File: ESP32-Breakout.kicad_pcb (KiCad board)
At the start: 2 copper layers, 44.5 x 49.5 mm, 3 parts, among them J101 Conn_01x19, J102 Conn_01x19, U101 ESP32-DEVKITC-32D

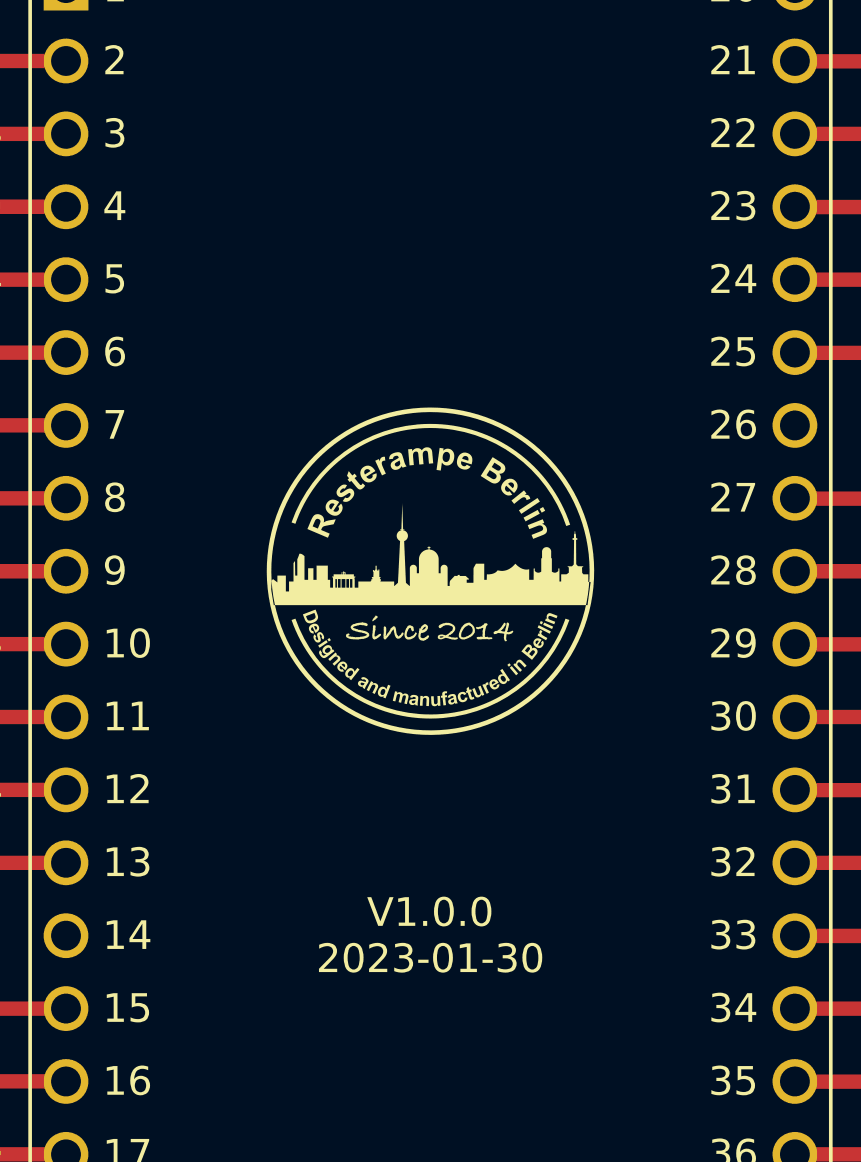
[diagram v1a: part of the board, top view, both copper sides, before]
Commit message: Documentation update, name of board on PCB
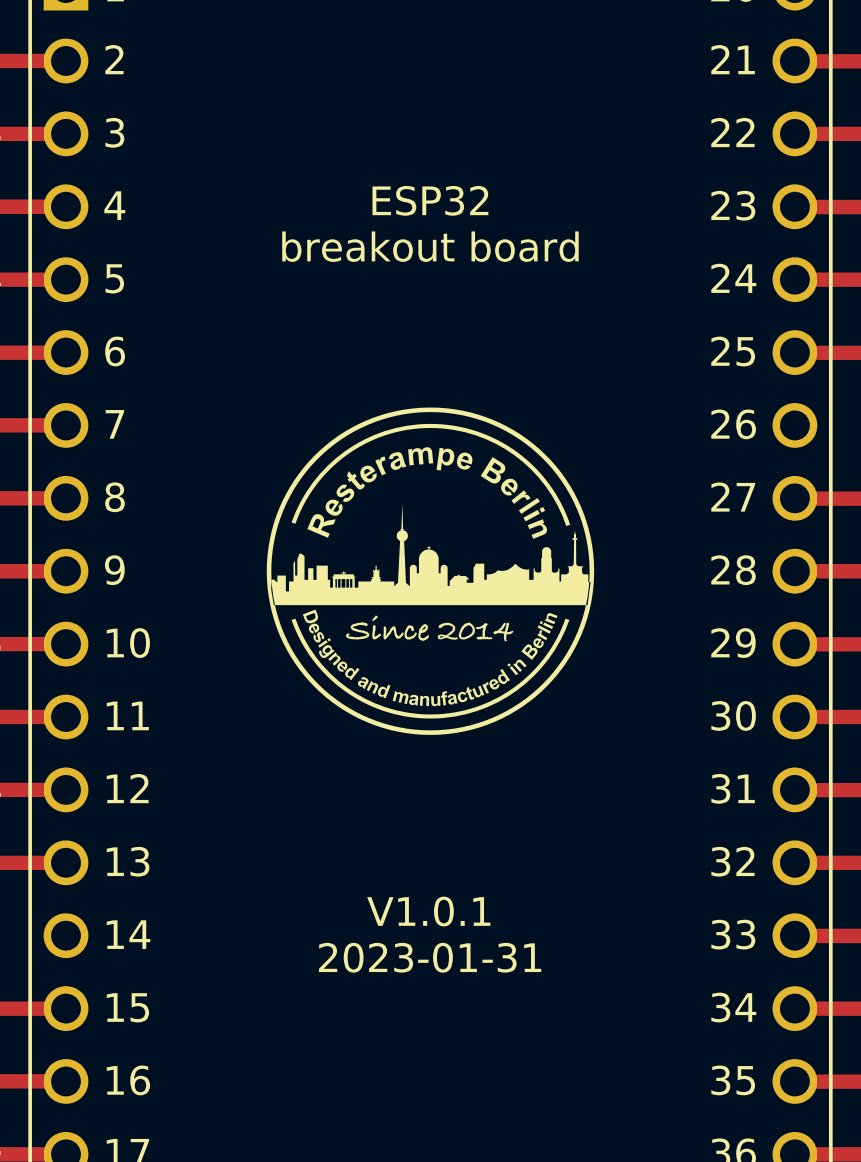
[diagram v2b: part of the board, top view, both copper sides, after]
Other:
- board text added: "ESP32 breakout board"
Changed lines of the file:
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@@
   (title_block
     (title "ESP32 Breakout board")
-    (date "2023-01-30")
-    (rev "1.0.0")
+    (date "2023-01-31")
+    (rev "1.0.1")
     (company "Resterampe Berlin ")
     (comment 3 "https://creativecommons.org/licenses/by-nc/4.0 ")
@@
     (effects (font (size 1 1) (thickness 0.15)))
   )
+  (gr_text "ESP32\nbreakout board" (at 160.02 81.915) (layer "F.SilkS")
+    (effects (font (size 1 1) (thickness 0.15)))
+  )

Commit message: Added 3D stacking header
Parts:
- U101: footprint Module:MODULE_ESP32-DEVKITC-32D -> ESP32:MODULE_ESP32-DEVKITC-32D
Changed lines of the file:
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@@
       (layer "F.SilkS" (type "Top Silk Screen"))
       (layer "F.Paste" (type "Top Solder Paste"))
-      (layer "F.Mask" (type "Top Solder Mask") (thickness 0.01))
+      (layer "F.Mask" (type "Top Solder Mask") (color "Purple") (thickness 0.01))
       (layer "F.Cu" (type "copper") (thickness 0.035))
       (layer "dielectric 1" (type "core") (thickness 1.51) (material "FR4") (epsilon_r 4.5) (loss_tangent 0.02))
       (layer "B.Cu" (type "copper") (thickness 0.035))
-      (layer "B.Mask" (type "Bottom Solder Mask") (thickness 0.01))
+      (layer "B.Mask" (type "Bottom Solder Mask") (color "Purple") (thickness 0.01))
       (layer "B.Paste" (type "Bottom Solder Paste"))
       (layer "B.SilkS" (type "Bottom Silk Screen"))
@@
     )
   )
-  (footprint "Module:MODULE_ESP32-DEVKITC-32D" (layer "F.Cu")
+  (footprint "ESP32:MODULE_ESP32-DEVKITC-32D" (layer "F.Cu")
     (at 160.02 93.42)
     (property "MANUFACTURER" "Espressif Systems")
@@
       (effects (font (size 1.000386 1.000386) (thickness 0.15)))
     )
-    (fp_text value "ESP32-DEVKITC-32D" (at 1.24136 28.294535) (layer "F.Fab") hide
+    (fp_text value "ESP32-DEVKITC-32D" (at 1.24136 28.294535) (layer "F.Fab")
       (effects (font (size 1.001047 1.001047) (thickness 0.15)))
     )
     (fp_line (start -13.95 -27.15) (end 13.95 -27.15) (layer "F.SilkS") (width 0.127))
+    (fp_line (start 13.95 27.25) (end -13.95 27.25) (layer "F.SilkS") (width 0.127))
     (fp_line (start 13.95 -27.15) (end 13.95 27.25) (layer "F.SilkS") (width 0.127))
     (fp_line (start -13.95 27.25) (end -13.95 -27.15) (layer "F.SilkS") (width 0.127))
-    (fp_line (start 13.95 27.25) (end -13.95 27.25) (layer "F.SilkS") (width 0.127))
+    (fp_line (start 14.2 -27.4) (end 14.2 27.5) (layer "F.CrtYd") (width 0.05))
     (fp_line (start -14.2 -27.4) (end 14.2 -27.4) (layer "F.CrtYd") (width 0.05))
     (fp_line (start 14.2 27.5) (end -14.2 27.5) (layer "F.CrtYd") (width 0.05))
     (fp_line (start -14.2 27.5) (end -14.2 -27.4) (layer "F.CrtYd") (width 0.05))
-    (fp_line (start 14.2 -27.4) (end 14.2 27.5) (layer "F.CrtYd") (width 0.05))
+    (fp_line (start -13.95 -27.15) (end 13.95 -27.15) (layer "F.Fab") (width 0.127))
+    (fp_line (start 13.95 -27.15) (end 13.95 27.25) (layer "F.Fab") (width 0.127))
     (fp_line (start 13.95 27.25) (end -13.95 27.25) (layer "F.Fab") (width 0.127))
     (fp_line (start -13.95 27.25) (end -13.95 -27.15) (layer "F.Fab") (width 0.127))
-    (fp_line (start 13.95 -27.15) (end 13.95 27.25) (layer "F.Fab") (width 0.127))
-    (fp_line (start -13.95 -27.15) (end 13.95 -27.15) (layer "F.Fab") (width 0.127))
     (fp_circle (center -14.6 -19.9) (end -14.46 -19.9) (layer "F.Fab") (width 0.28) (fill none))
     (fp_circle (center -14.6 -19.9) (end -14.46 -19.9) (layer "F.Fab") (width 0.28) (fill none))
@@
     (pad "38" thru_hole circle (at 12.7 25.96) (size 1.56 1.56) (drill 1.04) (layers *.Cu *.Mask)
       (net 36 "Net-(J102-Pad19)") (pinfunction "CLK") (pintype "input"))
+    (model "${KIPRJMOD}/Stacking header_19x1_25.4mm.step"
+      (offset (xyz -12.7 -25.9 0))
+      (scale (xyz 1 1 1))
+      (rotate (xyz -90 0 -90))
+    )
   )
   (gr_poly

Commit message: Names streamlined
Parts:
- U101: footprint ESP32:MODULE_ESP32-DEVKITC-32D -> ESP32:MODULE_ESP32-DEVKITC-32D_Stacking_header_TH
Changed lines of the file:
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@@
     )
   )
-  (footprint "ESP32:MODULE_ESP32-DEVKITC-32D" (layer "F.Cu")
+  (footprint "ESP32:MODULE_ESP32-DEVKITC-32D_Stacking_header_TH" (layer "F.Cu")
     (at 160.02 93.42)
     (property "MANUFACTURER" "Espressif Systems")
@@
     (fp_line (start -13.95 -27.15) (end 13.95 -27.15) (layer "F.SilkS") (width 0.127))
     (fp_line (start 13.95 27.25) (end -13.95 27.25) (layer "F.SilkS") (width 0.127))
+    (fp_line (start -13.95 27.25) (end -13.95 -27.15) (layer "F.SilkS") (width 0.127))
     (fp_line (start 13.95 -27.15) (end 13.95 27.25) (layer "F.SilkS") (width 0.127))
-    (fp_line (start -13.95 27.25) (end -13.95 -27.15) (layer "F.SilkS") (width 0.127))
     (fp_line (start 14.2 -27.4) (end 14.2 27.5) (layer "F.CrtYd") (width 0.05))
     (fp_line (start -14.2 -27.4) (end 14.2 -27.4) (layer "F.CrtYd") (width 0.05))
+    (fp_line (start -14.2 27.5) (end -14.2 -27.4) (layer "F.CrtYd") (width 0.05))
     (fp_line (start 14.2 27.5) (end -14.2 27.5) (layer "F.CrtYd") (width 0.05))
-    (fp_line (start -14.2 27.5) (end -14.2 -27.4) (layer "F.CrtYd") (width 0.05))
     (fp_line (start -13.95 -27.15) (end 13.95 -27.15) (layer "F.Fab") (width 0.127))
+    (fp_line (start -13.95 27.25) (end -13.95 -27.15) (layer "F.Fab") (width 0.127))
     (fp_line (start 13.95 -27.15) (end 13.95 27.25) (layer "F.Fab") (width 0.127))
     (fp_line (start 13.95 27.25) (end -13.95 27.25) (layer "F.Fab") (width 0.127))
-    (fp_line (start -13.95 27.25) (end -13.95 -27.15) (layer "F.Fab") (width 0.127))
     (fp_circle (center -14.6 -19.9) (end -14.46 -19.9) (layer "F.Fab") (width 0.28) (fill none))
     (fp_circle (center -14.6 -19.9) (end -14.46 -19.9) (layer "F.Fab") (width 0.28) (fill none))
@@
     (pad "38" thru_hole circle (at 12.7 25.96) (size 1.56 1.56) (drill 1.04) (layers *.Cu *.Mask)
       (net 36 "Net-(J102-Pad19)") (pinfunction "CLK") (pintype "input"))
-    (model "${KIPRJMOD}/Stacking header_19x1_25.4mm.step"
+    (model "${KIPRJMOD}/Stacking header 2x19_25.4mm.step"
       (offset (xyz -12.7 -25.9 0))
       (scale (xyz 1 1 1))

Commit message: Closed #1
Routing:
- net Net-(J102-Pad8): track 7.62 -> 10.2 mm
- net Net-(J102-Pad6): track 7.62 -> 10.2 mm
- net Net-(J102-Pad5): track 7.62 -> 10.2 mm
- net Net-(J102-Pad4): track 7.62 -> 10.2 mm
- net Net-(J102-Pad3): track 7.62 -> 10.2 mm
- net Net-(J102-Pad19): track 7.62 -> 10.2 mm
- net Net-(J102-Pad17): track 7.62 -> 10.2 mm
- net Net-(J102-Pad15): track 7.62 -> 10.2 mm
- net Net-(J102-Pad13): track 7.62 -> 10.2 mm
- net Net-(J102-Pad12): track 7.62 -> 10.2 mm
- net Net-(J102-Pad10): track 7.62 -> 10.2 mm
- net Net-(J102-Pad9): track 7.62 -> 10.2 mm
- net Net-(J102-Pad2): track 7.62 -> 10.2 mm
- net Net-(J102-Pad18): track 7.62 -> 10.2 mm
- net Net-(J102-Pad16): track 7.62 -> 10.2 mm
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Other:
- board text added: "This is the smaller 32S board (fits well on breadboard)"
- board text added: "This is the wider 32D board"
